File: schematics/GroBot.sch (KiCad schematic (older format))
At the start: 78 parts

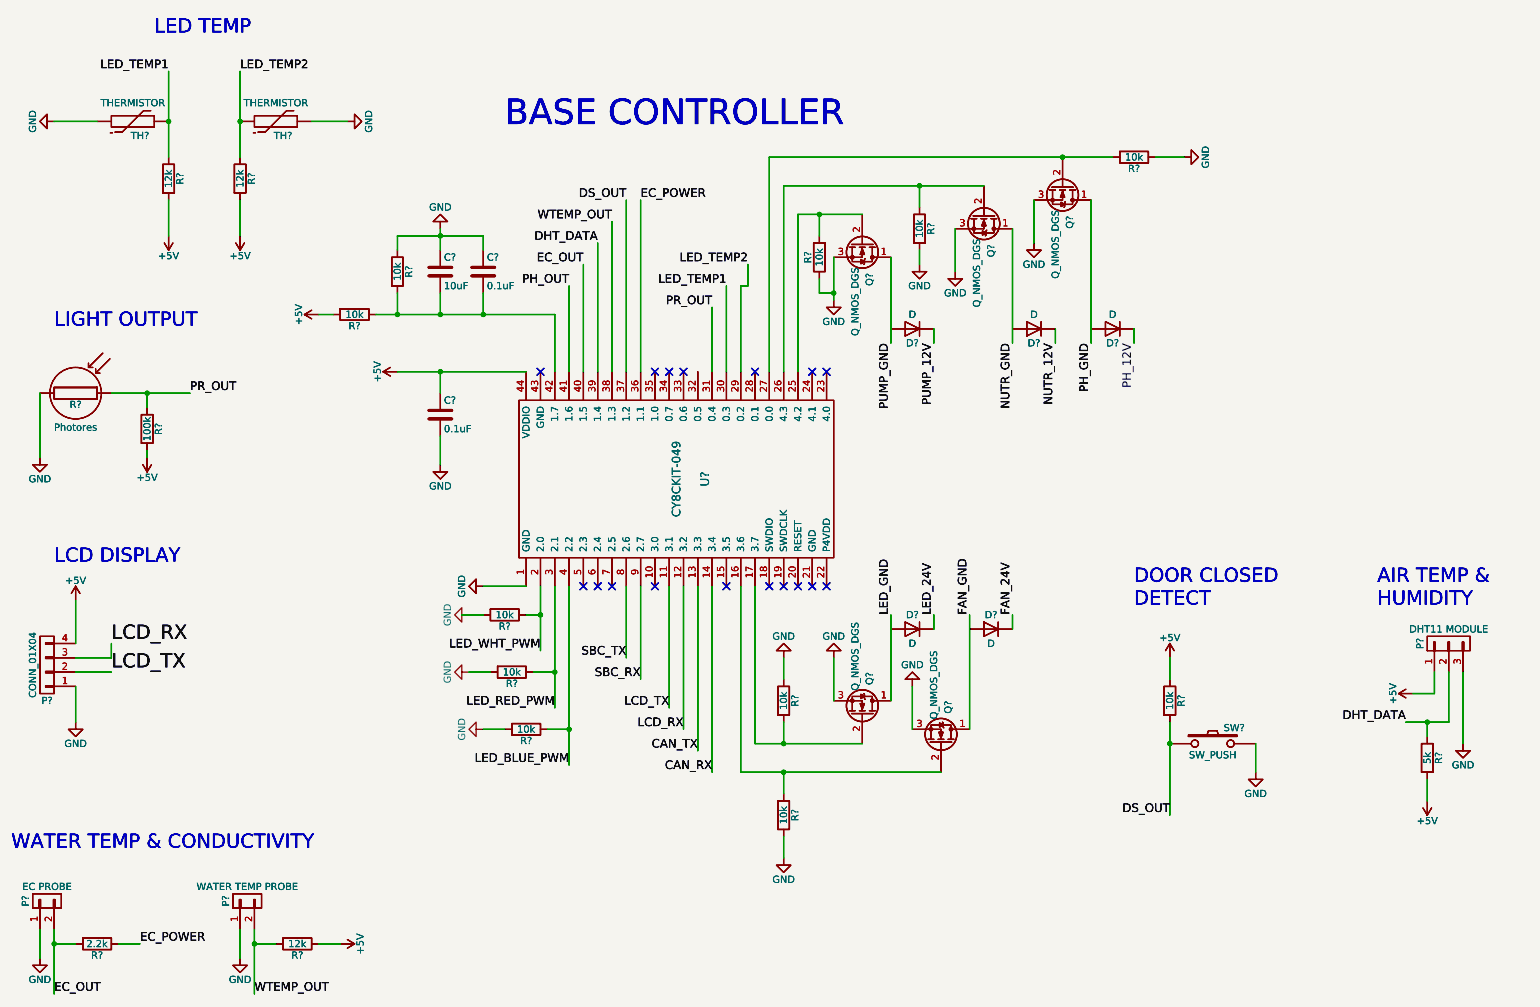
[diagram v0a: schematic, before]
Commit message: Added I2C labels, fixed duplicate components fixes #4
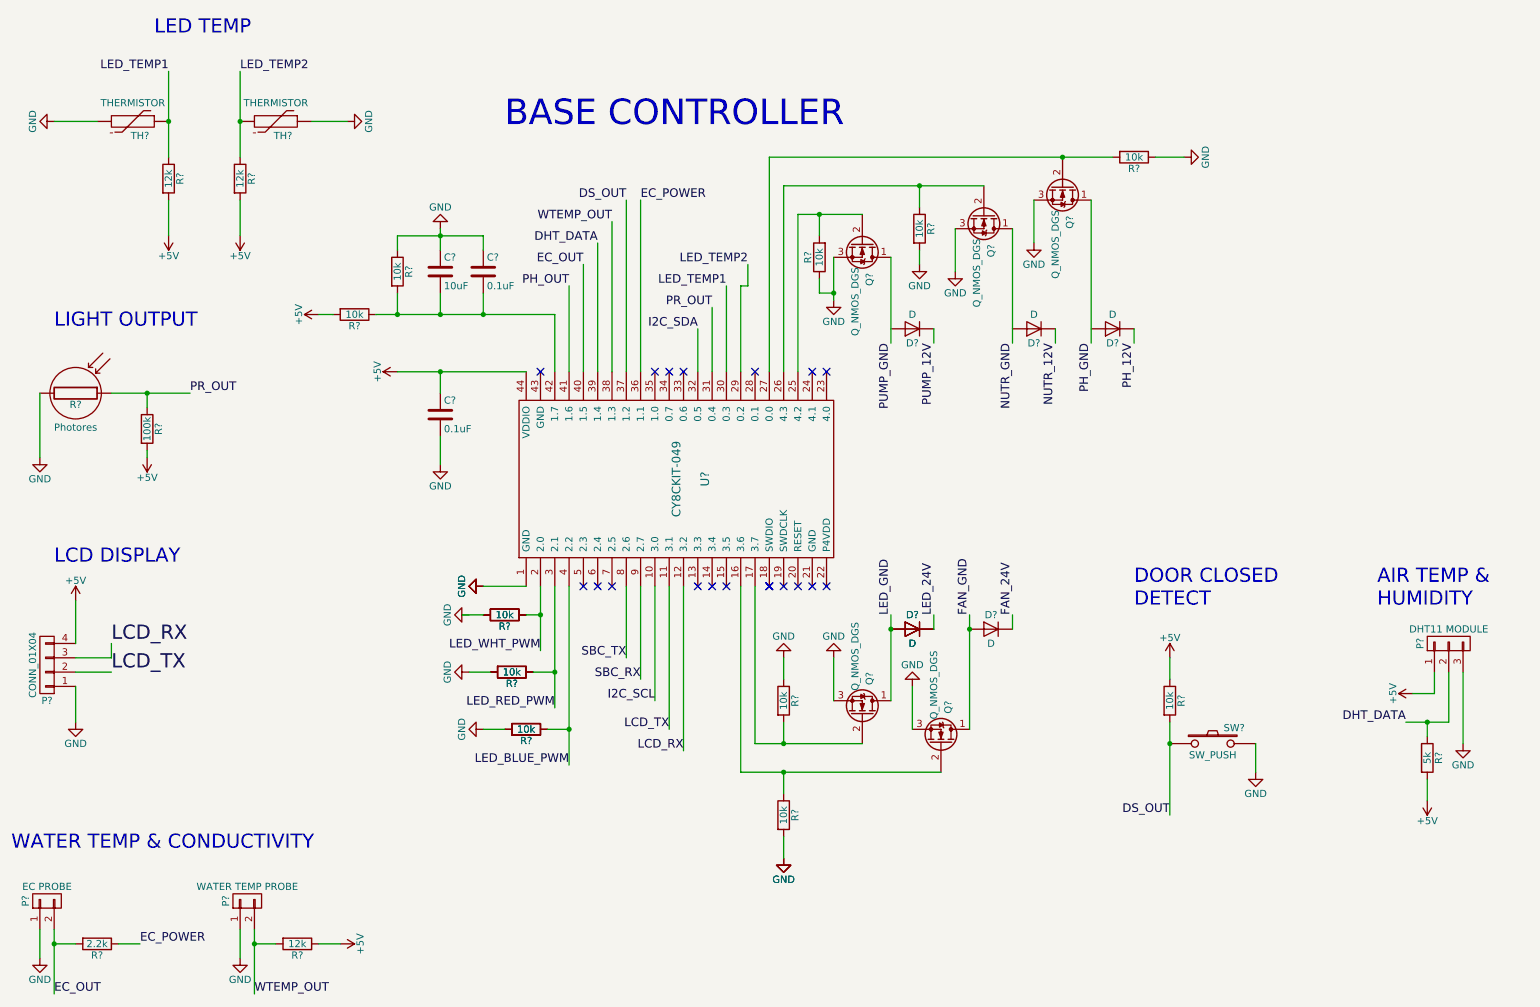
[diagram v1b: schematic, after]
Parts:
- removed C?: 10uF, symbol C
- removed C? (x2): 0.1uF, symbol C
- removed D? (x4): D, symbol D
- removed P?: EC PROBE, symbol CONN_01X02
- removed P?: WATER TEMP PROBE, symbol CONN_01X02
- removed P?: DHT11 MODULE, symbol CONN_01X03
- removed P?: CONN_01X04, symbol CONN_01X04
- removed Q? (x5): Q_NMOS_DGS, symbol Q_NMOS_DGS
- removed R? (x8): 10k, symbol R
- removed R? (x3): 12k, symbol R
- removed R?: 2.2k, symbol R
- removed R?: 5k, symbol R
- removed R?: Photores, symbol Photores
- removed R?: 100k, symbol R
- removed SW?: SW_PUSH, symbol SW_PUSH
- removed TH? (x2): THERMISTOR, symbol THERMISTOR
- removed U?: CY8CKIT-049, symbol CY8CKIT-049
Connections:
- net FAN_GND: now also D?.2 (A)
- net LED_GND: now also D?.2 (A), D?.2 (A)
- net I2C_SCL: now reaches U?.10 (3.0)
- net I2C_SDA: now reaches U?.32 (0.5)
- net CAN_RX: no longer names the net of U?.14 (3.4)
- net CAN_TX: no longer names the net of U?.13 (3.3)
- no-connect marks 34 -> 19
